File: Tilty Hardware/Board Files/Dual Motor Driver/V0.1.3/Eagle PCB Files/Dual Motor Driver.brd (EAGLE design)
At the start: 38.4 x 50.8 mm, 42 parts, among them J1 AVR_SPI_PRG_62X3_LOCK, Q1 16MHz, U1 ATMEGA328P, U2 L298_BRIDGE_DRIVER, U3 LM2931

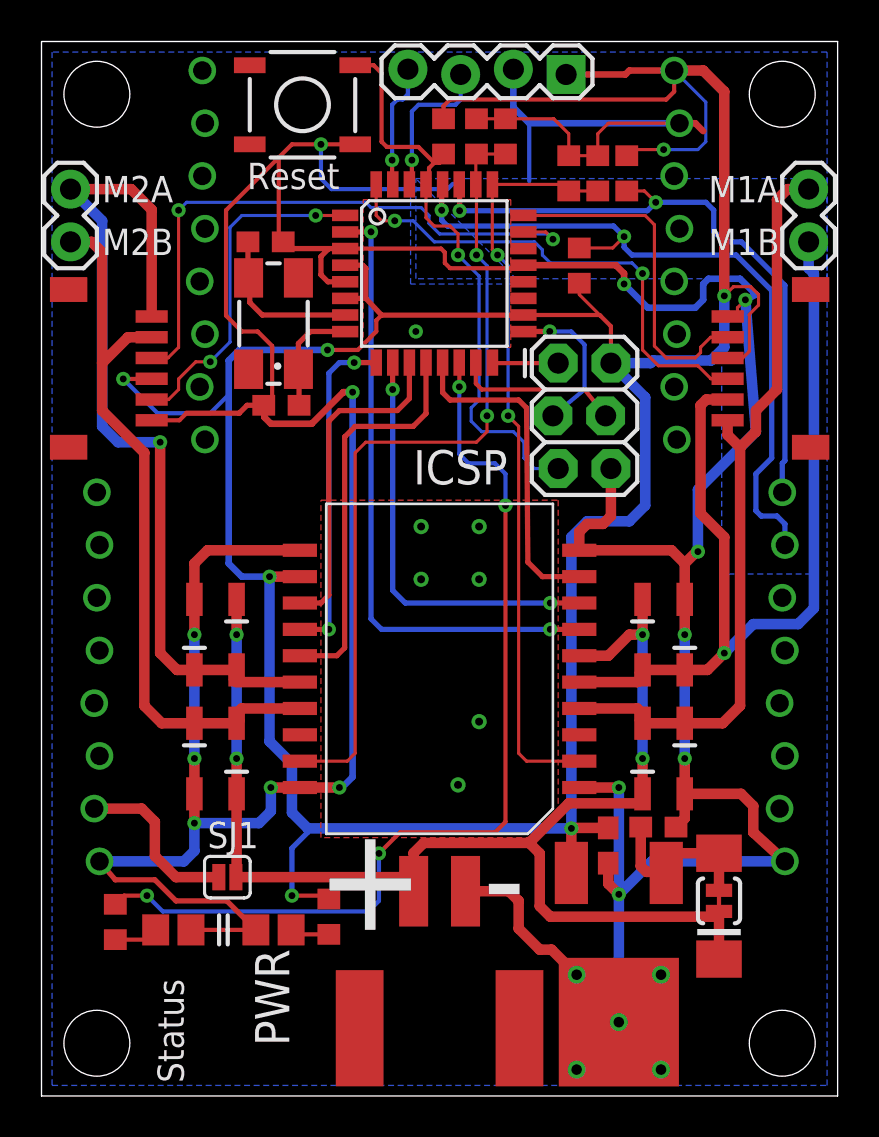
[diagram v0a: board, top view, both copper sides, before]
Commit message: Increased ground plane on Dual Motor Driver for heat dissipation
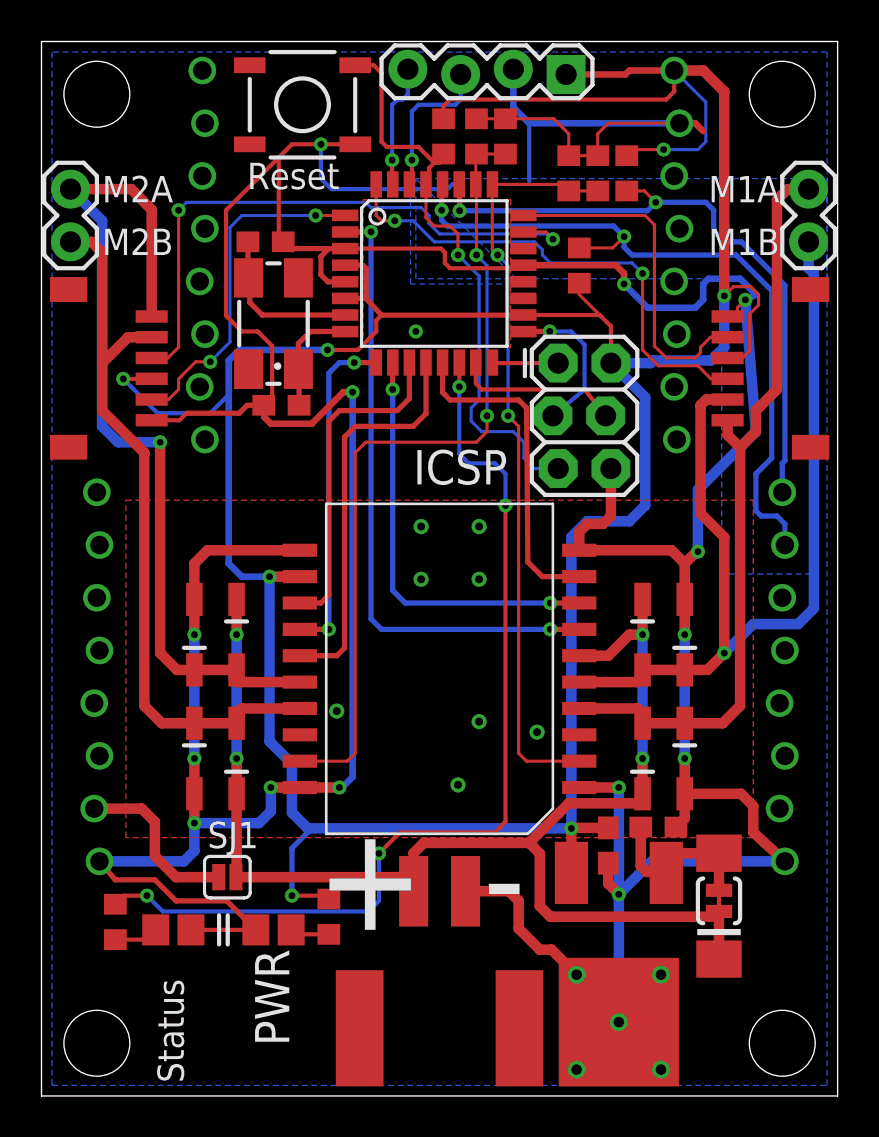
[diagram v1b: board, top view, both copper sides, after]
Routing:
- net GND: vias 26 -> 28
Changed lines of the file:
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@@
 <wire x1="3.556" y1="10.414" x2="2.794" y2="11.303" width="0.254" layer="1"/>
 <polygon width="0.2032" layer="1">
-<vertex x="13.462" y="28.702"/>
-<vertex x="24.892" y="28.702"/>
-<vertex x="24.892" y="13.716"/>
-<vertex x="23.622" y="12.446"/>
-<vertex x="13.462" y="12.446"/>
+<vertex x="4.064" y="28.702"/>
+<vertex x="34.29" y="28.702"/>
+<vertex x="34.29" y="12.446"/>
+<vertex x="4.064" y="12.446"/>
 </polygon>
 <wire x1="30.988" y1="14.556" x2="30.988" y2="13.374" width="0.508" layer="1"/>
@@
 </polygon>
 <via x="18.034" y="36.83" extent="1-16" drill="0.3302"/>
+<via x="23.876" y="17.526" extent="1-16" drill="0.381"/>
+<via x="14.224" y="18.542" extent="1-16" drill="0.381"/>
 </signal>
 <signal name="M1A">
